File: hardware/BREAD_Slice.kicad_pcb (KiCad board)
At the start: 2 copper layers, 72.6 x 100 mm, 16 parts, among them J1 Conn_01x10_Female, J2 I2C_01x04

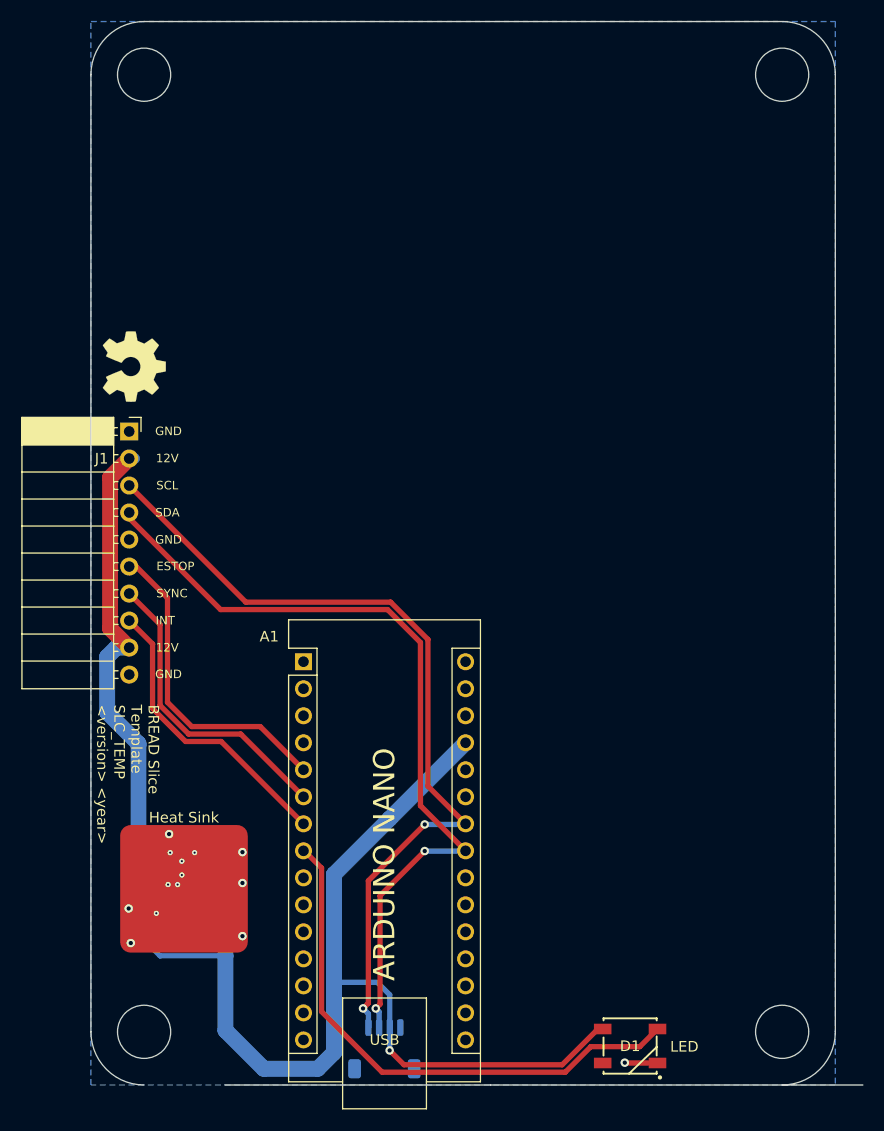
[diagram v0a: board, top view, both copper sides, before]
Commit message: updated + checked schem and pcb with updated template
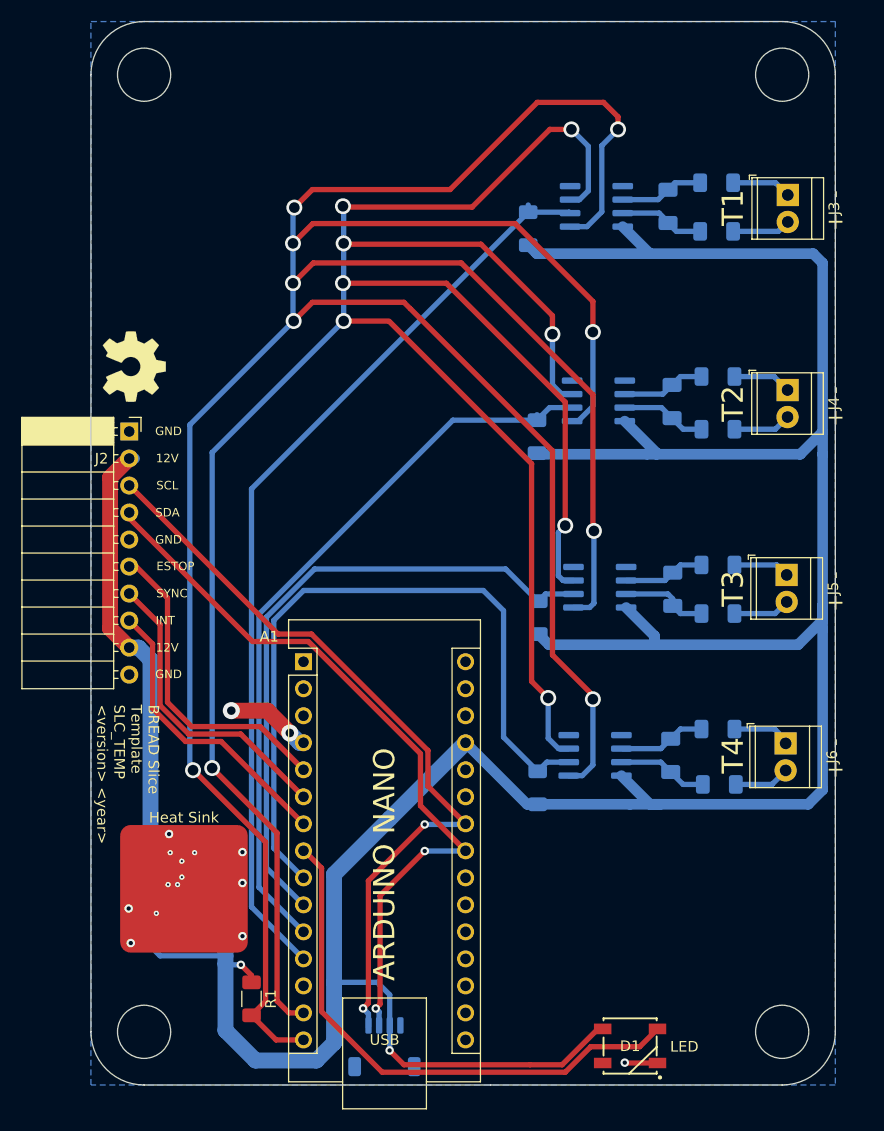
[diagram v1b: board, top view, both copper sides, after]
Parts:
- added C5: 0.01 uF, Capacitor_SMD:C_1206_3216Metric_Pad1.33x1.80mm_HandSolder, B.Cu at (176.9, 57.2)
- added C6: 0.01 uF, Capacitor_SMD:C_1206_3216Metric_Pad1.33x1.80mm_HandSolder, B.Cu at (177.2, 75.5)
- added C7: 0.01 uF, Capacitor_SMD:C_1206_3216Metric_Pad1.33x1.80mm_HandSolder, B.Cu at (177.3, 93.2)
- added C8: 0.01 uF, Capacitor_SMD:C_1206_3216Metric_Pad1.33x1.80mm_HandSolder, B.Cu at (177.1, 108.8)
- added FB1: Ferrite_Bead_Small, Resistor_SMD:R_1206_3216Metric_Pad1.30x1.75mm_HandSolder, B.Cu at (181.4, 59.5)
- added FB2: Ferrite_Bead_Small, Resistor_SMD:R_1206_3216Metric_Pad1.30x1.75mm_HandSolder, B.Cu at (181.4, 55.0)
- added FB3: Ferrite_Bead_Small, Resistor_SMD:R_1206_3216Metric_Pad1.30x1.75mm_HandSolder, B.Cu at (181.6, 78.1)
- added FB4: Ferrite_Bead_Small, Resistor_SMD:R_1206_3216Metric_Pad1.30x1.75mm_HandSolder, B.Cu at (181.6, 73.2)
- added FB5: Ferrite_Bead_Small, Resistor_SMD:R_1206_3216Metric_Pad1.30x1.75mm_HandSolder, B.Cu at (181.6, 95.5)
- added FB6: Ferrite_Bead_Small, Resistor_SMD:R_1206_3216Metric_Pad1.30x1.75mm_HandSolder, B.Cu at (181.6, 90.9)
- added FB7: Ferrite_Bead_Small, Resistor_SMD:R_1206_3216Metric_Pad1.30x1.75mm_HandSolder, B.Cu at (181.7, 111.5)
- added FB8: Ferrite_Bead_Small, Resistor_SMD:R_1206_3216Metric_Pad1.30x1.75mm_HandSolder, B.Cu at (181.6, 106.3)
- added J3: Screw_Terminal_01x02, TerminalBlock_TE-Connectivity:TerminalBlock_TE_282834-2_1x02_P2.54mm_Horizontal, F.Cu at (188.1, 56.1)
- added J4: Screw_Terminal_01x02, TerminalBlock_TE-Connectivity:TerminalBlock_TE_282834-2_1x02_P2.54mm_Horizontal, F.Cu at (188.1, 74.5)
- added J5: Screw_Terminal_01x02, TerminalBlock_TE-Connectivity:TerminalBlock_TE_282834-2_1x02_P2.54mm_Horizontal, F.Cu at (188.0, 91.8)
- added J6: Screw_Terminal_01x02, TerminalBlock_TE-Connectivity:TerminalBlock_TE_282834-2_1x02_P2.54mm_Horizontal, F.Cu at (187.9, 107.7)
- added R1: 10k, Resistor_SMD:R_1206_3216Metric_Pad1.30x1.75mm_HandSolder, F.Cu at (137.7, 131.7)
- added R2: 10k, Resistor_SMD:R_1206_3216Metric_Pad1.30x1.75mm_HandSolder, B.Cu at (163.7, 59.3)
- added R3: 10k, Resistor_SMD:R_1206_3216Metric_Pad1.30x1.75mm_HandSolder, B.Cu at (164.5, 78.8)
- added R4: 10k, Resistor_SMD:R_1206_3216Metric_Pad1.30x1.75mm_HandSolder, B.Cu at (164.7, 95.9)
- added R5: 10k, Resistor_SMD:R_1206_3216Metric_Pad1.30x1.75mm_HandSolder, B.Cu at (164.6, 111.9)
- added U2: MAX31855KASA, Package_SO:SOIC-8_3.9x4.9mm_P1.27mm, B.Cu at (170.1, 57.2)
- added U3: MAX31855KASA, Package_SO:SOIC-8_3.9x4.9mm_P1.27mm, B.Cu at (170.3, 75.5)
- added U4: MAX31855KASA, Package_SO:SOIC-8_3.9x4.9mm_P1.27mm, B.Cu at (170.5, 93.0)
- added U5: MAX31855KASA, Package_SO:SOIC-8_3.9x4.9mm_P1.27mm, B.Cu at (170.0, 108.8)
- HS1: footprint SparkFun-Fuse:Thermal Pad -> KML-Custom:Thermal Pad
- moved J1 0.20 mm to (150.2, 136.2)
- renumbered J2 to J1, J1 to J2
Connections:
- A1 pad 10: unconnected-(A1-D7-Pad10) -> /SS3
- A1 pad 11: unconnected-(A1-D8-Pad11) -> /SS2
- A1 pad 12: unconnected-(A1-D9-Pad12) -> /SS1
- A1 pad 14: unconnected-(A1-D11-Pad14) -> /DATA
- A1 pad 15: unconnected-(A1-D12-Pad15) -> /CLK
- A1 pad 9: unconnected-(A1-D6-Pad9) -> /SS4
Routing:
- net /CLK: track 0.00 -> 303.3 mm, vias 0 -> 9
- net /DATA: track 0.00 -> 246.4 mm, vias 0 -> 9
- net +5V: track 108.9 -> 300.2 mm, vias 1 -> 2
- net /SS1: track 0.00 -> 87.7 mm
- net /SS2: track 0.00 -> 69.6 mm
- net /SS4: track 0.00 -> 69.1 mm
- net /SS3: track 0.00 -> 60.8 mm
- net Net-(U5-T+): track 0.00 -> 8.53 mm
- net Net-(U5-T-): track 0.00 -> 8.29 mm
- net Net-(U4-T+): track 0.00 -> 8.24 mm
- net Net-(U3-T+): track 0.00 -> 8.06 mm
- net Net-(U2-T+): track 0.00 -> 8.05 mm
- net GND: track 19.6 -> 27.7 mm, vias 14 -> 16
- net Net-(U2-T-): track 0.00 -> 7.94 mm
- net Net-(U3-T-): track 0.00 -> 7.90 mm
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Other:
- board size 72.6 x 100 mm -> 70 x 100 mm
- board text added: "+"
- board text added: "-"
- board text added: "T1"
- board text added: "T2"
- board text added: "T3"
- board text added: "T4"

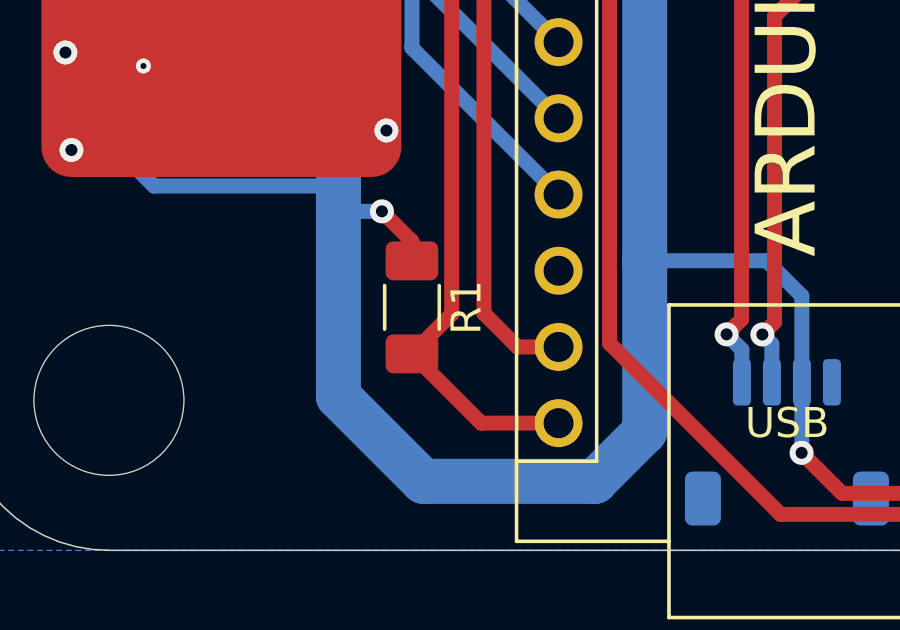
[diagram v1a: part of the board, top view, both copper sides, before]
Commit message: removed unneeded top level 10k clk pull up (one on each max already
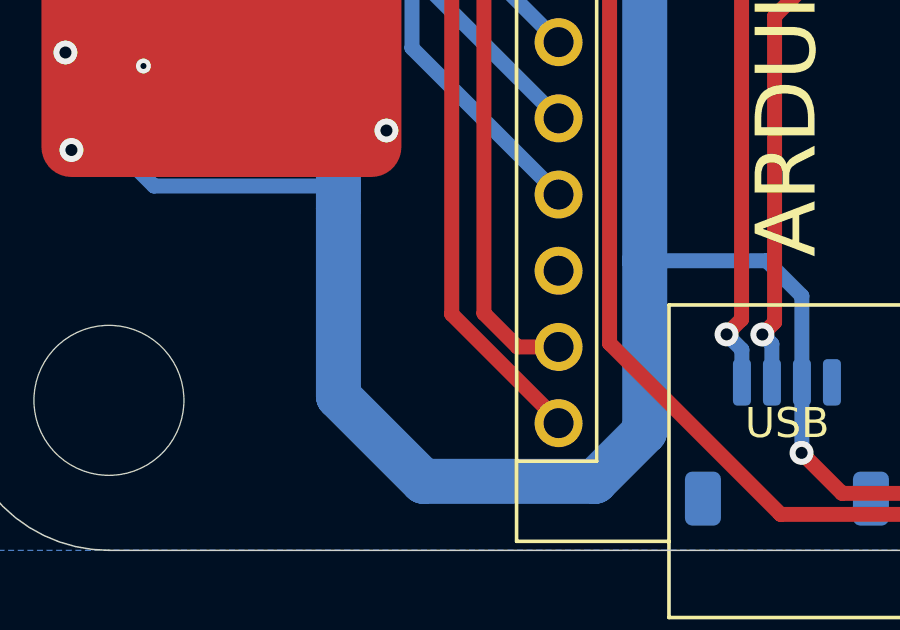
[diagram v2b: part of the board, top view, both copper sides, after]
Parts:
- removed R1: 10k, Resistor_SMD:R_1206_3216Metric_Pad1.30x1.75mm_HandSolder
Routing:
- net +5V: track 300.2 -> 296.8 mm, vias 2 -> 1
- net /CLK: track 303.3 -> 300.7 mm
